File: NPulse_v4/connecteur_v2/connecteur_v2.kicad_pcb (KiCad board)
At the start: 4 copper layers, 39.8 x 51 mm, 26 parts, among them J1 Conn_01x02_Socket, J10 Conn_02x05_Odd_Even, J13 Conn_02x05_Odd_Even, J2 Conn_01x02_Socket, J23 Conn_01x01, J24 Conn_01x06_Socket, J25 Conn_01x06_Socket, J26 Conn_01x06_Socket, J27 Conn_01x01, J28 Conn_01x06_Socket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

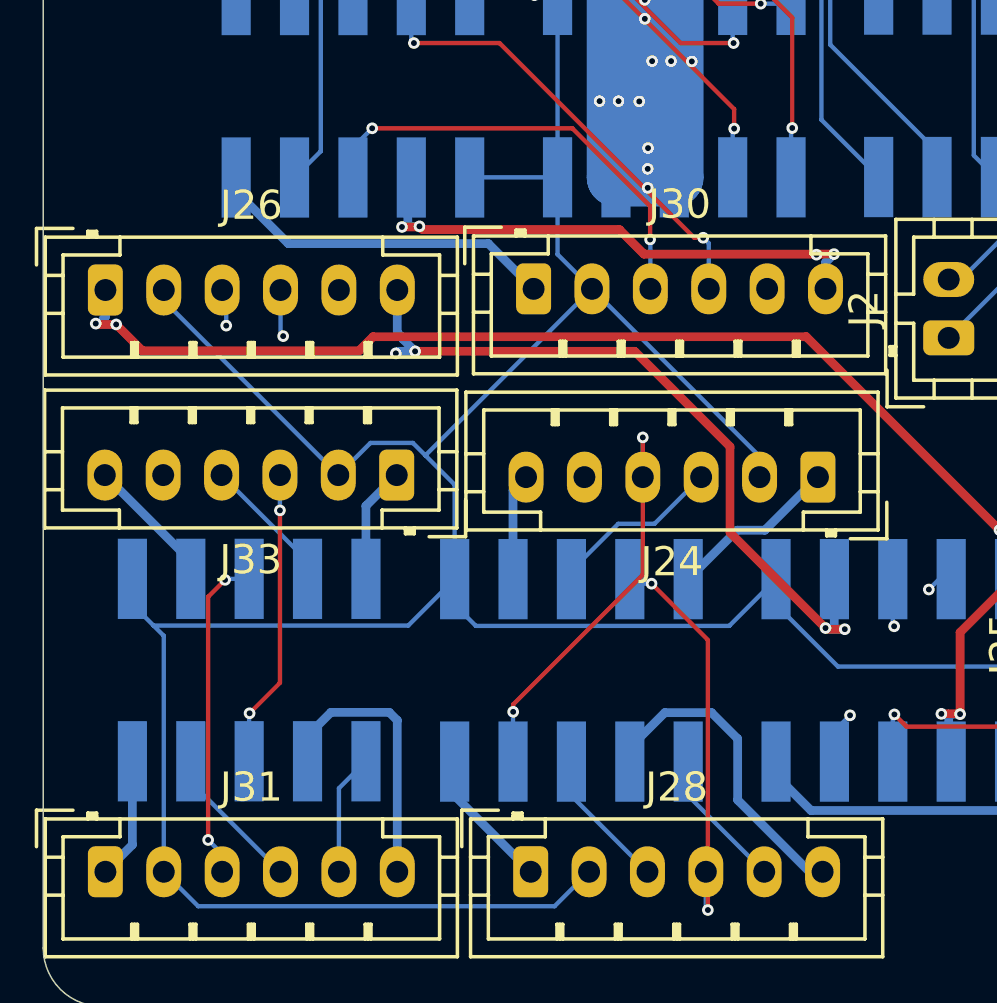
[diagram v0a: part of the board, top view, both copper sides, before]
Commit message: add some via on Hat for emi
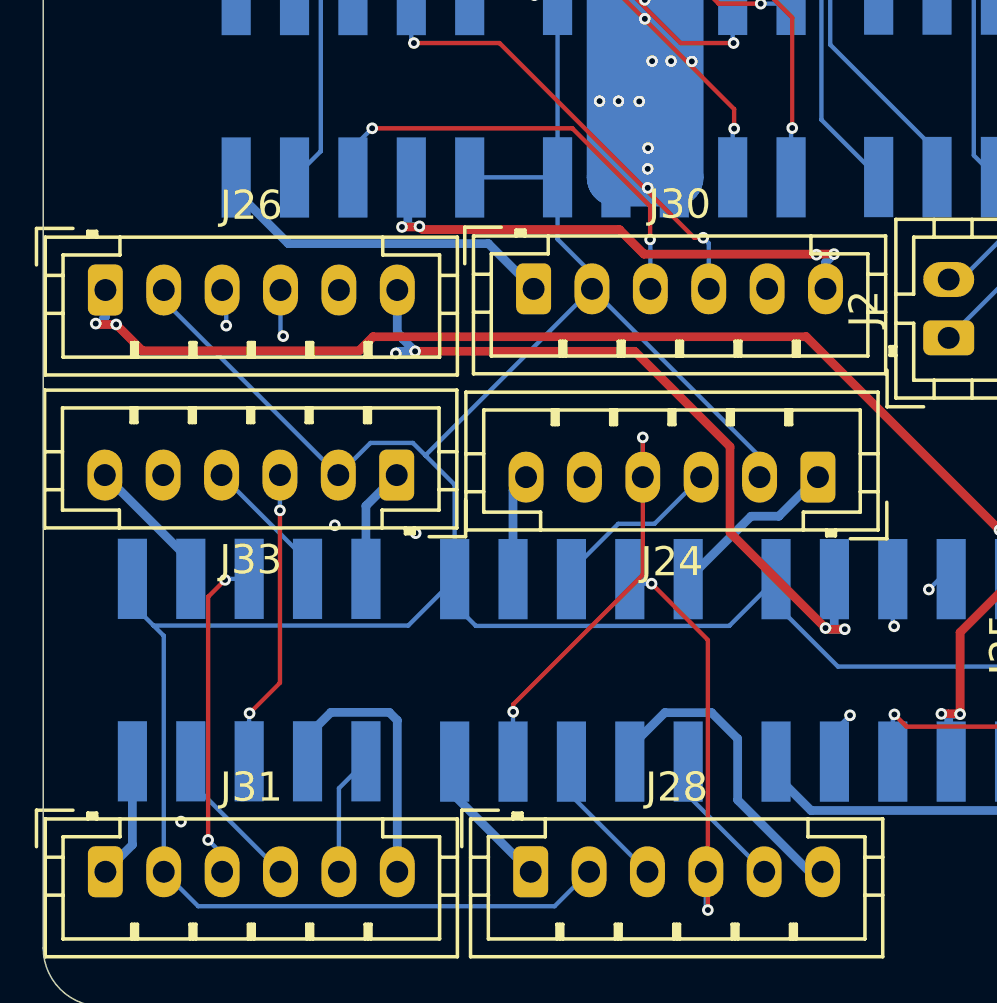
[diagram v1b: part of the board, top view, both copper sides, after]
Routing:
- net GND: vias 3 -> 6
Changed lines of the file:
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@@
+	)
+	(via
+		(at 158.1 131.31)
+		(size 0.4)
+		(drill 0.2)
+		(layers "F.Cu" "B.Cu")
+		(free yes)
+		(net 2)
 	)
 	(via
@@
 	(via
 		(at 170.4 95.34)
+		(size 0.4)
+		(drill 0.2)
+		(layers "F.Cu" "B.Cu")
+		(free yes)
+		(net 2)
+	)
+	(via
+		(at 163.37 121.16)
+		(size 0.4)
+		(drill 0.2)
+		(layers "F.Cu" "B.Cu")
+		(free yes)
+		(net 2)
+	)
+	(via
+		(at 166.14 121.43)
 		(size 0.4)
 		(drill 0.2)
@@
 	)
 	(segment
+		(start 171 109.24)
+		(end 171 111.36)
+		(width 0.15)
+		(layer "B.Cu")
+		(net 6)
+	)
+	(segment
 		(start 177.919999 119.51)
 		(end 177.919999 118.799998)
@@
 	)
 	(segment
-		(start 171 111.879999)
-		(end 172.180001 113.06)
-		(width 0.15)
-		(layer "B.Cu")
-		(net 6)
-	)
-	(segment
 		(start 157.161 124.596)
 		(end 165.884 124.596)
@@
 	)
 	(segment
+		(start 171 111.36)
+		(end 172.180001 112.540001)
+		(width 0.15)
+		(layer "B.Cu")
+		(net 6)
+	)
+	(segment
 		(start 166.487547 118.782453)
 		(end 166.044094 118.339)
@@
 	)
 	(segment
-		(start 171 109.24)
-		(end 171 111.879999)
-		(width 0.15)
-		(layer "B.Cu")
-		(net 6)
-	)
-	(segment
 		(start 178.485 123.88)
 		(end 178.485 123.005)
@@
 	)
 	(segment
+		(start 172.180001 112.540001)
+		(end 172.180001 113.06)
+		(width 0.15)
+		(layer "B.Cu")
+		(net 6)
+	)
+	(segment
 		(start 159.65 113.24)
 		(end 159.51 113.1)
@@
 	)
 	(segment
-		(start 177.151 121.329)
-		(end 178.101 121.329)
+		(start 177.63 120.85)
+		(end 178.58 120.85)
 		(width 0.3)
 		(layer "B.Cu")
@@
 	)
 	(segment
-		(start 178.101 121.329)
+		(start 175.475 123.005)
+		(end 177.63 120.85)
+		(width 0.3)
+		(layer "B.Cu")
+		(net 32)
+	)
+	(segment
+		(start 178.58 120.85)
 		(end 179.92 119.51)
 		(width 0.3)
 		(layer "B.Cu")
-		(net 32)
-	)
-	(segment
-		(start 175.475 123.005)
-		(end 177.151 121.329)
-		(width 0.3)
-		(layer "B.Cu")
